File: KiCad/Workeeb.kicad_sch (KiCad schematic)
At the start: 201 parts, among them U1 EFM32HG322F64G-C-QFP48

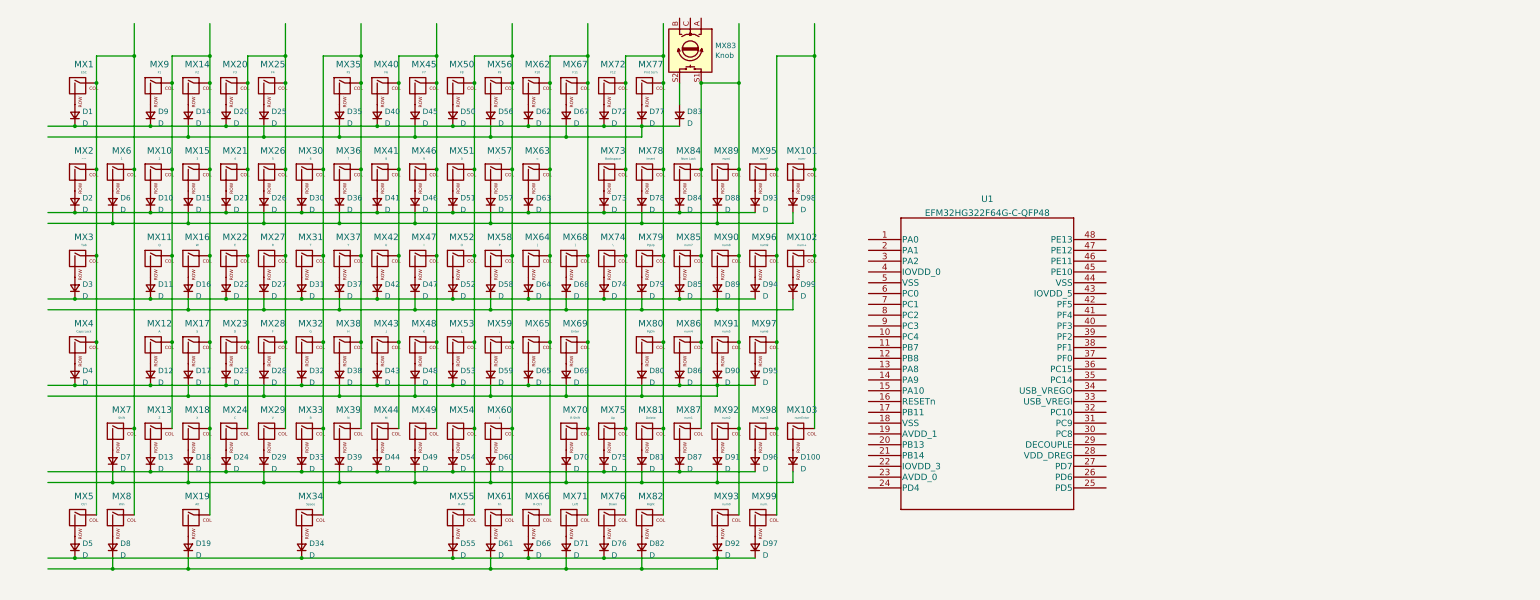
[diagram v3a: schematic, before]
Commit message: Begin lengthy process of hooking up switches/designing power circuitry
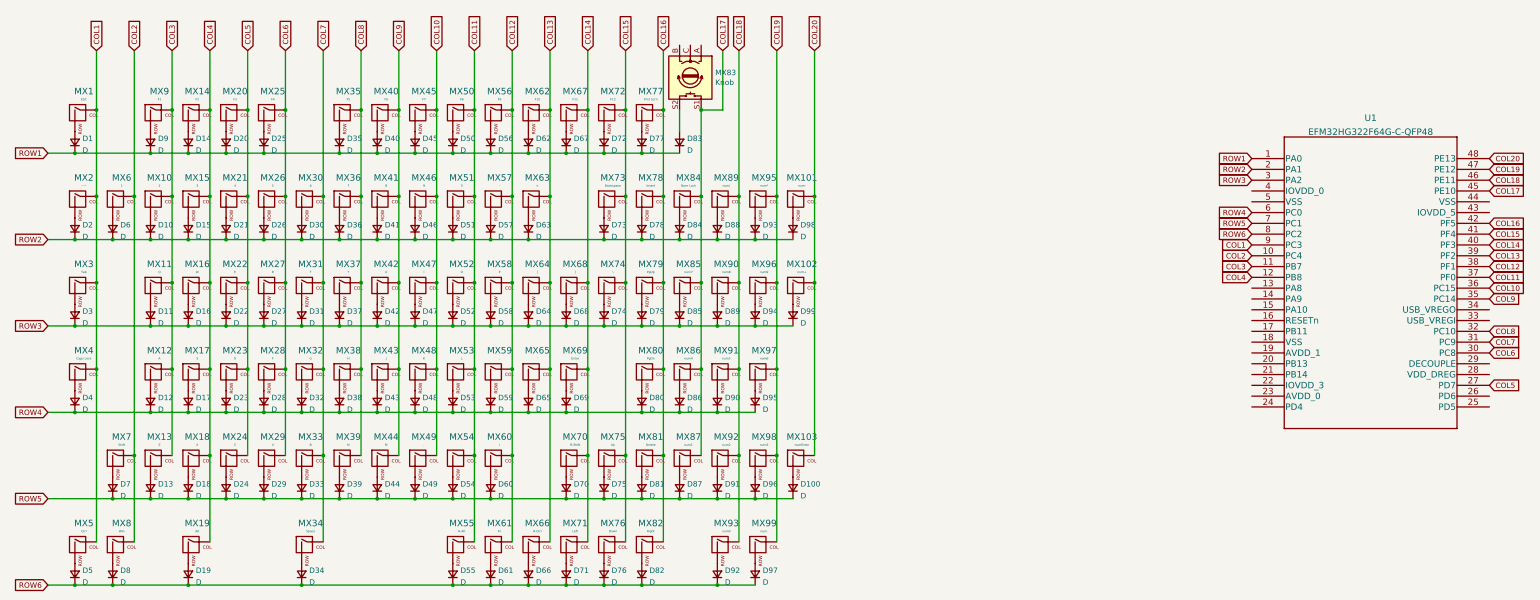
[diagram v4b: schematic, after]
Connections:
- net COL1: now reaches MX1.1 (COL), MX2.1 (COL), MX3.1 (COL), MX4.1 (COL), MX5.1 (COL)
- net COL1: now also U1.9 (PC3); no longer MX6.1 (COL), MX7.1 (COL), MX8.1 (COL)
- net COL4: now reaches MX14.1 (COL), MX15.1 (COL), MX16.1 (COL), MX17.1 (COL), MX18.1 (COL), MX19.1 (COL)
- net COL4: now also U1.12 (PB8); no longer MX10.1 (COL), MX11.1 (COL), MX12.1 (COL), MX13.1 (COL), MX9.1 (COL)
- net COL5: now reaches MX20.1 (COL), MX21.1 (COL), MX22.1 (COL), MX23.1 (COL), MX24.1 (COL)
- net COL5: now also U1.27 (PD7); no longer MX25.1 (COL), MX26.1 (COL), MX27.1 (COL), MX28.1 (COL), MX29.1 (COL)
- net COL7: now reaches MX30.1 (COL), MX31.1 (COL), MX32.1 (COL), MX33.1 (COL), MX34.1 (COL)
- net COL7: now also U1.31 (PC9); no longer MX35.1 (COL), MX36.1 (COL), MX37.1 (COL), MX38.1 (COL), MX39.1 (COL)
- net COL10: now reaches MX45.1 (COL), MX46.1 (COL), MX47.1 (COL), MX48.1 (COL), MX49.1 (COL)
- net COL10: now also U1.36 (PC15); no longer MX40.1 (COL), MX41.1 (COL), MX42.1 (COL), MX43.1 (COL), MX44.1 (COL)
- net COL11: now reaches MX50.1 (COL), MX51.1 (COL), MX52.1 (COL), MX53.1 (COL), MX54.1 (COL), MX55.1 (COL)
- net COL11: now also U1.37 (PF0); no longer MX56.1 (COL), MX57.1 (COL), MX58.1 (COL), MX59.1 (COL), MX60.1 (COL), MX61.1 (COL)
- net COL13: now reaches MX62.1 (COL), MX63.1 (COL), MX64.1 (COL), MX65.1 (COL), MX66.1 (COL)
- net COL13: now also U1.39 (PF2); no longer MX67.1 (COL), MX68.1 (COL), MX69.1 (COL), MX70.1 (COL), MX71.1 (COL)
- net COL16: now reaches MX77.1 (COL), MX78.1 (COL), MX79.1 (COL), MX80.1 (COL), MX81.1 (COL), MX82.1 (COL)
- net COL16: now also U1.42 (PF5); no longer MX72.1 (COL), MX73.1 (COL), MX74.1 (COL), MX75.1 (COL), MX76.1 (COL)
- net COL17: now reaches MX83.S1, MX84.1 (COL), MX85.1 (COL), MX86.1 (COL), MX87.1 (COL)
- net COL17: now also U1.45 (PE10); no longer MX89.1 (COL), MX90.1 (COL), MX91.1 (COL), MX92.1 (COL), MX93.1 (COL)
- net COL19: now reaches MX95.1 (COL), MX96.1 (COL), MX97.1 (COL), MX98.1 (COL), MX99.1 (COL)
- net COL19: now also U1.47 (PE12); no longer MX101.1 (COL), MX102.1 (COL), MX103.1 (COL)
- net ROW5: now reaches D100.1 (K), D18.1 (K), D29.1 (K), D39.1 (K), D49.1 (K), D60.1 (K), D7.1 (K), D70.1 (K), D81.1 (K), D91.1 (K)
- net ROW5: now also D13.1 (K), D24.1 (K), D33.1 (K), D44.1 (K), D54.1 (K), D75.1 (K), D87.1 (K), D96.1 (K), U1.7 (PC1)
- net ROW1: now reaches D1.1 (K), D14.1 (K), D20.1 (K), D25.1 (K), D35.1 (K), D40.1 (K), D45.1 (K), D50.1 (K), D56.1 (K), D62.1 (K), D67.1 (K), D72.1 (K), D77.1 (K), D83.1 (K), D9.1 (K)
- net ROW1: now also U1.1 (PA0)
- net ROW2: now reaches D10.1 (K), D2.1 (K), D21.1 (K), D30.1 (K), D41.1 (K), D51.1 (K), D63.1 (K), D73.1 (K), D84.1 (K), D93.1 (K)
- net ROW2: now also D15.1 (K), D26.1 (K), D36.1 (K), D46.1 (K), D57.1 (K), D6.1 (K), D78.1 (K), D88.1 (K), D98.1 (K), U1.2 (PA1)
- net ROW3: now reaches D16.1 (K), D27.1 (K), D37.1 (K), D47.1 (K), D58.1 (K), D68.1 (K), D79.1 (K), D89.1 (K), D99.1 (K)
- net ROW3: now also D11.1 (K), D22.1 (K), D3.1 (K), D31.1 (K), D42.1 (K), D52.1 (K), D64.1 (K), D74.1 (K), D85.1 (K), D94.1 (K), U1.3 (PA2)
- net ROW6: now reaches D19.1 (K), D34.1 (K), D5.1 (K), D55.1 (K), D61.1 (K), D66.1 (K), D71.1 (K), D76.1 (K), D8.1 (K), D82.1 (K), D92.1 (K), D97.1 (K)
- net ROW6: now also U1.8 (PC2)
- net ROW4: now reaches D12.1 (K), D17.1 (K), D23.1 (K), D28.1 (K), D32.1 (K), D38.1 (K), D4.1 (K), D43.1 (K), D48.1 (K), D53.1 (K), D59.1 (K), D65.1 (K), D69.1 (K), D80.1 (K), D86.1 (K), D90.1 (K), D95.1 (K)
- net ROW4: now also U1.6 (PC0)
- net COL2: now reaches U1.10 (PC4)
- net COL2: now also MX6.1 (COL), MX7.1 (COL), MX8.1 (COL)
- net COL3: now reaches U1.11 (PB7)
- net COL3: now also MX10.1 (COL), MX11.1 (COL), MX12.1 (COL), MX13.1 (COL), MX9.1 (COL)
- net COL6: now reaches U1.30 (PC8)
- net COL6: now also MX25.1 (COL), MX26.1 (COL), MX27.1 (COL), MX28.1 (COL), MX29.1 (COL)
- net COL8: now reaches U1.32 (PC10)
- net COL8: now also MX35.1 (COL), MX36.1 (COL), MX37.1 (COL), MX38.1 (COL), MX39.1 (COL)
- net COL9: now reaches U1.35 (PC14)
- net COL9: now also MX40.1 (COL), MX41.1 (COL), MX42.1 (COL), MX43.1 (COL), MX44.1 (COL)
- net COL12: now reaches U1.38 (PF1)
- net COL12: now also MX56.1 (COL), MX57.1 (COL), MX58.1 (COL), MX59.1 (COL), MX60.1 (COL), MX61.1 (COL)
- net COL14: now reaches U1.40 (PF3)
- net COL14: now also MX67.1 (COL), MX68.1 (COL), MX69.1 (COL), MX70.1 (COL), MX71.1 (COL)
- net COL15: now reaches U1.41 (PF4)
- net COL15: now also MX72.1 (COL), MX73.1 (COL), MX74.1 (COL), MX75.1 (COL), MX76.1 (COL)
- net COL18: now reaches U1.46 (PE11)
- net COL18: now also MX89.1 (COL), MX90.1 (COL), MX91.1 (COL), MX92.1 (COL), MX93.1 (COL)
- net COL20: now reaches U1.48 (PE13)
- net COL20: now also MX101.1 (COL), MX102.1 (COL), MX103.1 (COL)
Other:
- moved on the sheet: D1, D10, D100, D11, D12, D13, D14, D15, D16, D17, D18, D19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

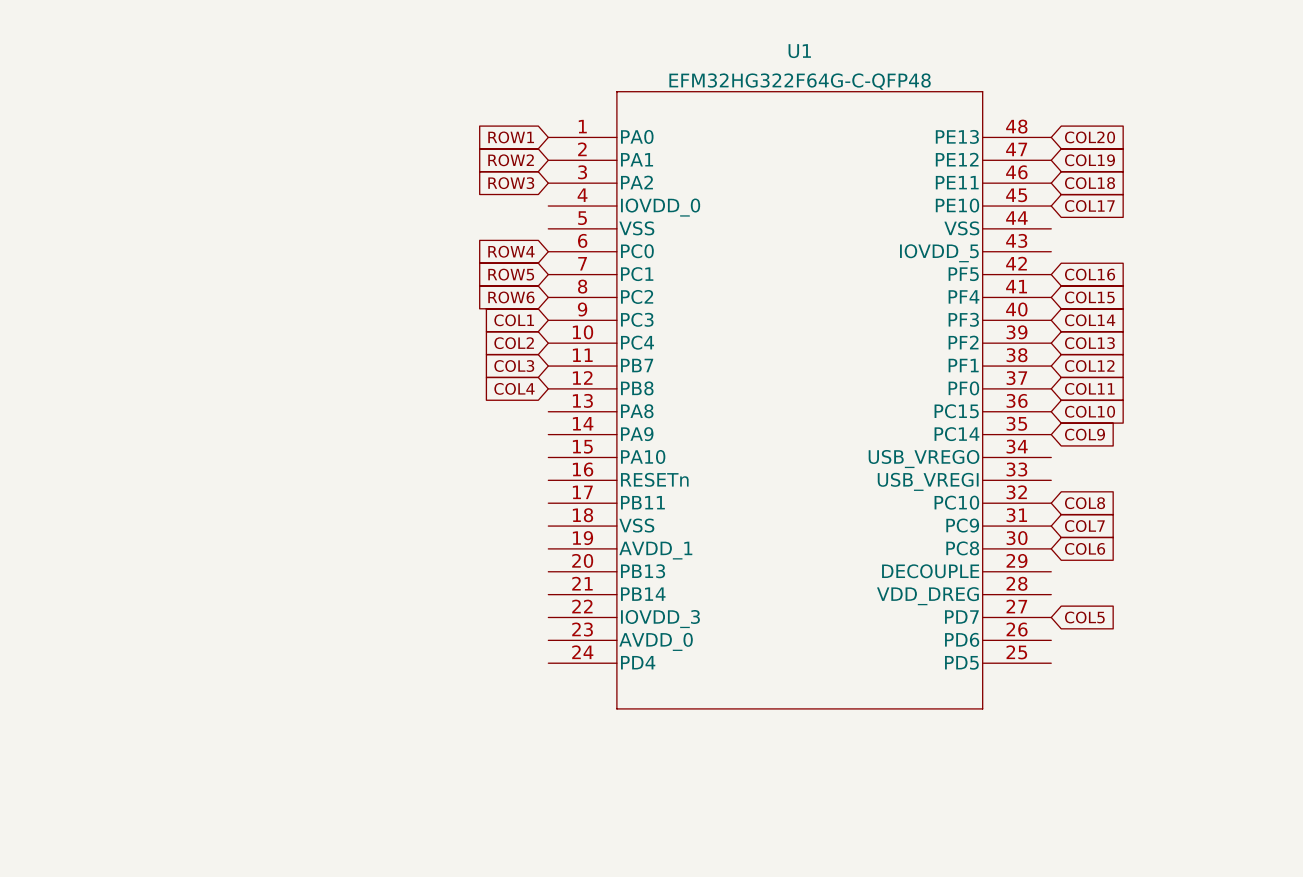
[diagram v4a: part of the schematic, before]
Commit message: start bad version of decoupling cap schema
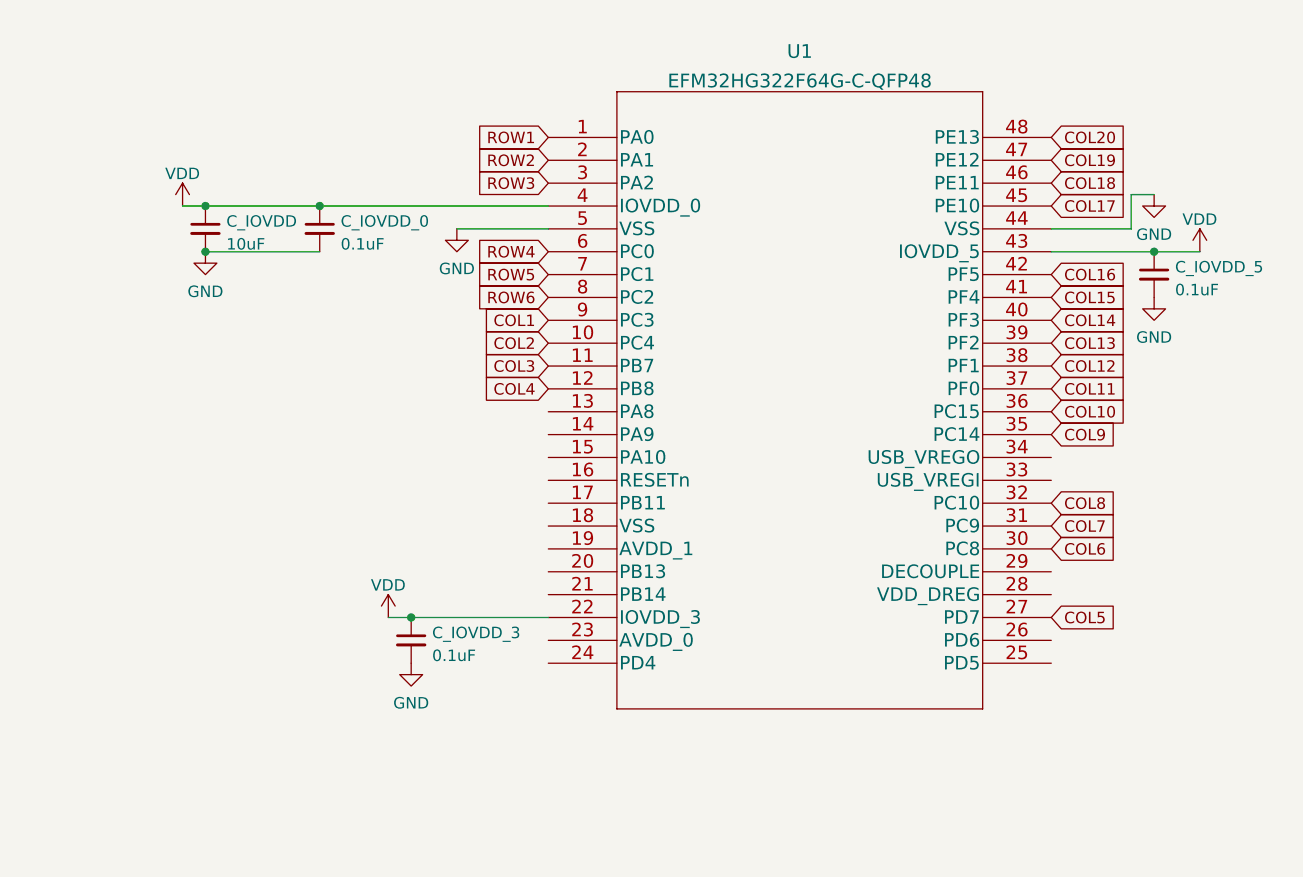
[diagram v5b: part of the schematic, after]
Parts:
- added C_IOVDD: 10uF, symbol Device:C_Small
- added C_IOVDD_0, C_IOVDD_3, C_IOVDD_5: 0.1uF, symbol Device:C_Small
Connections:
- net VDD: now reaches U1.22 (IOVDD_3)
- net VDD: now also U1.4 (IOVDD_0), U1.43 (IOVDD_5), C_IOVDD.1, C_IOVDD_0.1, C_IOVDD_3.1, C_IOVDD_5.1
- net GND: now reaches U1.44 (VSS)
- net GND: now also U1.5 (VSS), C_IOVDD.2, C_IOVDD_0.2, C_IOVDD_3.2, C_IOVDD_5.2

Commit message: Start proper power routing
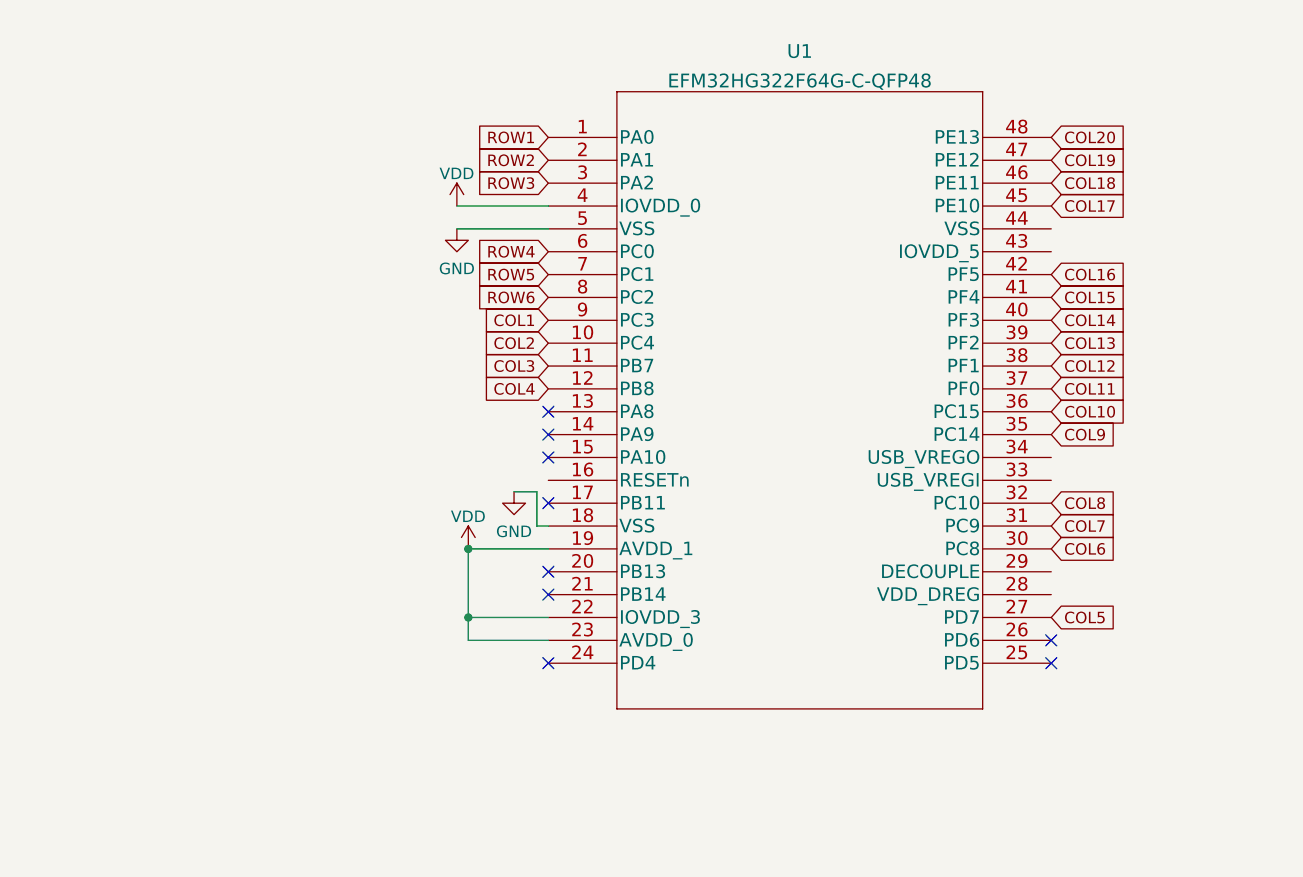
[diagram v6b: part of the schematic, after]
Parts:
- removed C_IOVDD: 10uF, symbol Device:C_Small
- removed C_IOVDD_0, C_IOVDD_3, C_IOVDD_5: 0.1uF, symbol Device:C_Small
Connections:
- net GND: now also U1.18 (VSS); no longer U1.44 (VSS)
- net VDD: now also U1.19 (AVDD_1), U1.23 (AVDD_0); no longer U1.43 (IOVDD_5)
- no-connect marks 0 -> 9
